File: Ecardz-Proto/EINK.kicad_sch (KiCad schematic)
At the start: 28 parts, among them J2 Conn_01x26, Q1 CSD16327Q3

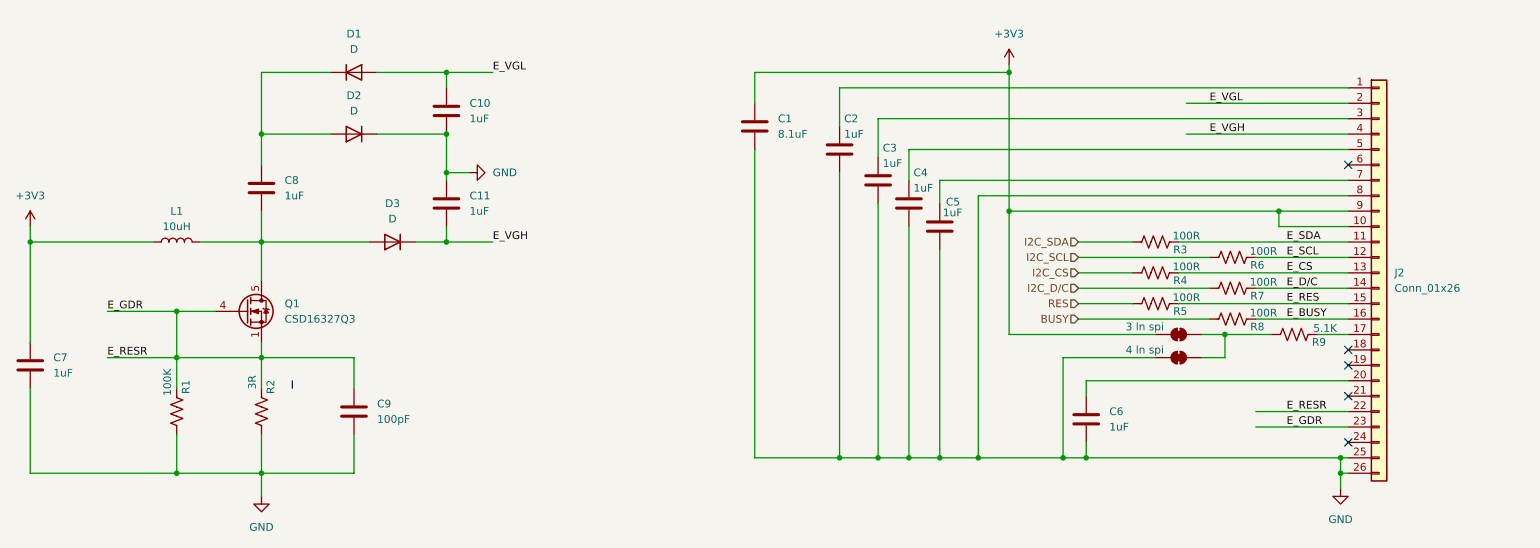
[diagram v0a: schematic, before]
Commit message: upated E-ink schematic
should be done - just missing inductor footprint
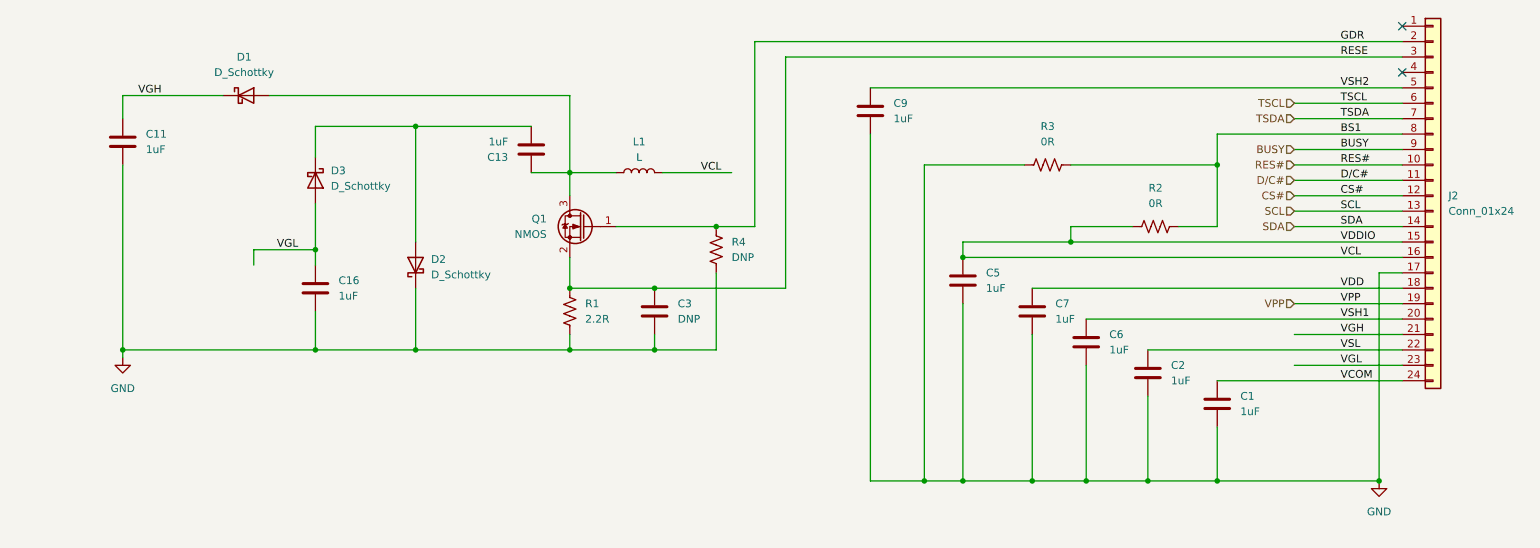
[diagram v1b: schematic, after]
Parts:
- removed C10, C4, C8: 1uF, symbol Device:C
- removed D1, D2, D3: D, symbol Device:D
- removed J2: Conn_01x26, symbol Connector_Generic:Conn_01x26
- removed JP1: 3 ln spi, symbol Jumper:SolderJumper_2_Bridged
- removed JP2: 4 ln spi, symbol Jumper:SolderJumper_2_Bridged
- removed Q1: CSD16327Q3, Package_SON:VSON-8_3.3x3.3mm_P0.65mm_NexFET, symbol Transistor_FET:CSD16327Q3
- removed R5, R6, R7, R8: 100R, symbol Device:R_US
- removed R9: 5.1K, symbol Device:R_US
- added C13, C16: 1uF, Capacitor_SMD:C_0603_1608Metric_Pad1.08x0.95mm_HandSolder, symbol Device:C
- added D1, D2, D3: D_Schottky, Diode_SMD:D_SOD-123, symbol Device:D_Schottky
- added J2: Conn_01x24, Connector_FFC-FPC:TE_2-1734839-4_1x24-1MP_P0.5mm_Horizontal, symbol Connector_Generic:Conn_01x24
- added Q1: NMOS, Package_TO_SOT_SMD:SOT-23, symbol Device:Q_NMOS_Depletion_GSD
- C1: value 8.1uF -> 1uF; footprint (none) -> Capacitor_SMD:C_0603_1608Metric_Pad1.08x0.95mm_HandSolder; MANUFACTURER PART NUMBER (none) -> CC0603KRX5R8BB105
- C11, C2, C5, C6, C7: footprint (none) -> Capacitor_SMD:C_0603_1608Metric_Pad1.08x0.95mm_HandSolder; MANUFACTURER PART NUMBER (none) -> CC0603KRX5R8BB105
- C3: value 1uF -> DNP; footprint (none) -> Capacitor_SMD:C_0603_1608Metric_Pad1.08x0.95mm_HandSolder; MANUFACTURER PART NUMBER (none) -> 100pF
- C9: value 100pF -> 1uF; footprint (none) -> Capacitor_SMD:C_0603_1608Metric_Pad1.08x0.95mm_HandSolder; MANUFACTURER PART NUMBER (none) -> CC0603KRX5R8BB105
- L1: value 10uH -> L; footprint (none) -> Inductor_SMD:L_Neosid_SM-PIC0602H; MANUFACTURER PART NUMBER (none) -> CDRH5D18NP-470NC
- R1: value 100K -> 2.2R; footprint (none) -> Resistor_SMD:R_0603_1608Metric_Pad0.98x0.95mm_HandSolder; MANUFACTURER PART NUMBER (none) -> RC0603FR-072R2L
- R2: value 3R -> 0R; footprint (none) -> Resistor_SMD:R_0603_1608Metric_Pad0.98x0.95mm_HandSolder; MANUFACTURER PART NUMBER (none) -> RC0603JR-070RL
- R3: value 100R -> 0R; footprint (none) -> Resistor_SMD:R_0603_1608Metric_Pad0.98x0.95mm_HandSolder; MANUFACTURER PART NUMBER (none) -> RC0603JR-070RL
- R4: value 100R -> DNP; footprint (none) -> Resistor_SMD:R_0603_1608Metric_Pad0.98x0.95mm_HandSolder; MANUFACTURER PART NUMBER (none) -> 100kR
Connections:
- net E_CS is gone; now on net GND: R4.2
- net E_VGH is gone; now on net GND: C11.2
- net I2C_SDA is gone; now on net GND: R3.1
- net BUSY: now also J2.9 (Pin_9)
- net GND: now also C1.2, R1.2, C16.2, D2.1 (K), J2.17 (Pin_17); no longer C1.1, C11.1, R1.1, R2.1
- net VCL: now reaches C5.1
- net VCL: now also L1.2, R2.1, J2.15 (Pin_15), J2.16 (Pin_16)
- net VSH1: now reaches C6.1
- net VSH1: now also J2.20 (Pin_20)
- net VSL: now reaches C2.1
- net VSL: now also J2.22 (Pin_22)
- net RESE: now reaches C3.1
- net RESE: now also R1.1, J2.3 (Pin_3), Q1.2 (S)
- removed net +3V3: C1.2, C7.1, L1.1
- removed net E_GDR: C9.1, R1.2, R2.2
- net E_SDA renamed BS1
- net BS1: now also R2.2, J2.8 (Pin_8)
- net I2C_CS renamed GDR
- net GDR: now also J2.2 (Pin_2), Q1.1 (G)
- new net: C13.1, D1.2 (A), L1.1, Q1.3 (D)
- new net: C13.2, D2.2 (A), D3.1 (K)
- new net CS#: J2.12 (Pin_12)
- new net D/C#: J2.11 (Pin_11)
- new net RES#: J2.10 (Pin_10)
- new net SCL: J2.13 (Pin_13)
- new net SDA: J2.14 (Pin_14)
- new net TSCL: J2.6 (Pin_6)
- new net TSDA: J2.7 (Pin_7)
- new net VCOM: C1.1, J2.24 (Pin_24)
- new net VDD: C7.1, J2.18 (Pin_18)
- new net VGH: C11.1, D1.1 (K), J2.21 (Pin_21)
- new net VGL: C16.1, D3.2 (A), J2.23 (Pin_23)
- new net VPP: J2.19 (Pin_19)
- new net VSH2: C9.1, J2.5 (Pin_5)
- no-connect marks 5 -> 2

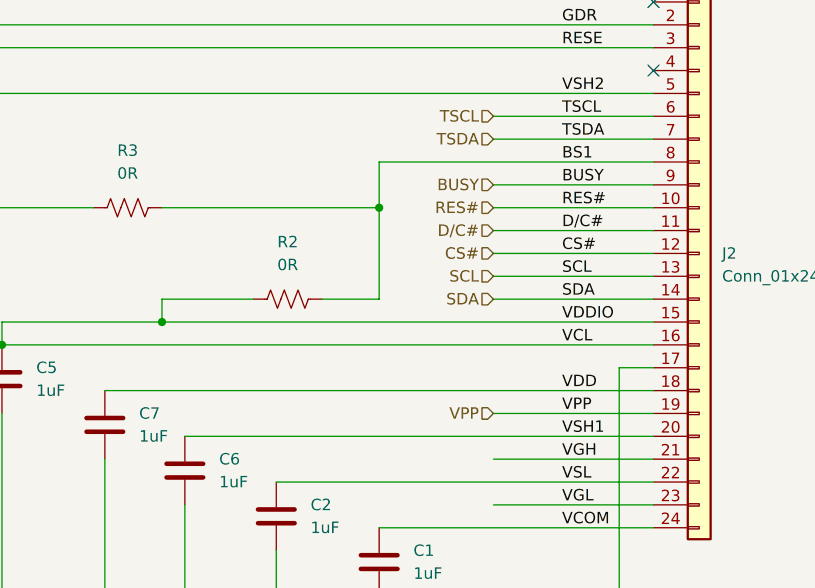
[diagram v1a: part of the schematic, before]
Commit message: added STM and rpi pin connections.
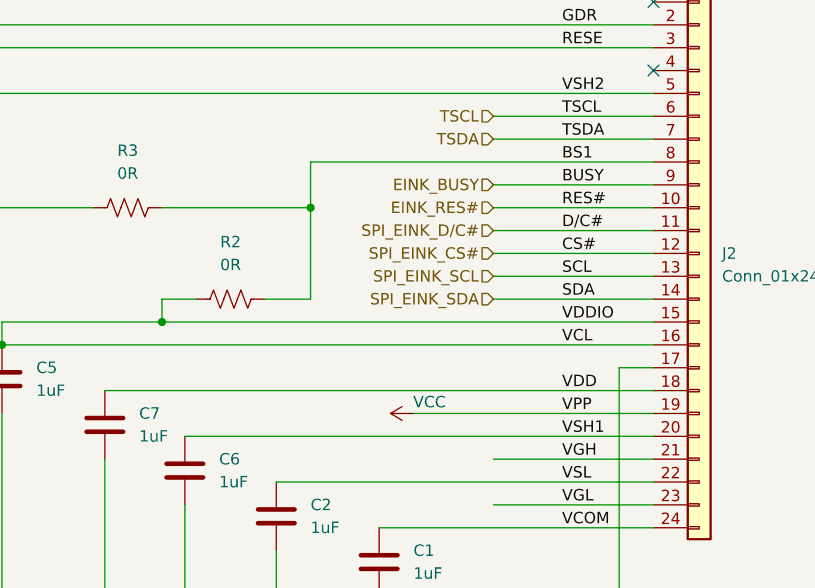
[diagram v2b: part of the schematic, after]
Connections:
- net BUSY renamed EINK_BUSY
- net CS# renamed SPI_EINK_CS#
- net D/C# renamed SPI_EINK_D/C#
- net RES# renamed EINK_RES#
- net SCL renamed SPI_EINK_SCL
- net SDA renamed SPI_EINK_SDA
- net VPP renamed VCC
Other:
- moved on the sheet: R2
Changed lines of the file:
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@@
 	)
 	(junction
+		(at 220.98 49.53)
+		(diameter 0)
+		(color 0 0 0 0)
+	)
+	(junction
 		(at 96.52 80.01)
 		(diameter 0)
@@
 	)
 	(junction
-		(at 228.6 49.53)
-		(diameter 0)
-		(color 0 0 0 0)
-	)
-	(junction
 		(at 255.27 101.6)
 		(diameter 0)
@@
 	(wire
 		(pts
-			(xy 214.63 59.69) (xy 204.47 59.69)
+			(xy 208.28 59.69) (xy 204.47 59.69)
 		)
 		(stroke
@@
 	(wire
 		(pts
-			(xy 204.47 49.53) (xy 228.6 49.53)
+			(xy 204.47 49.53) (xy 220.98 49.53)
 		)
 		(stroke
@@
 	(wire
 		(pts
-			(xy 241.3 72.39) (xy 259.08 72.39)
+			(xy 232.41 72.39) (xy 259.08 72.39)
 		)
 		(stroke
@@
 	(wire
 		(pts
-			(xy 228.6 44.45) (xy 259.08 44.45)
+			(xy 220.98 44.45) (xy 259.08 44.45)
 		)
 		(stroke
@@
 	(wire
 		(pts
-			(xy 222.25 59.69) (xy 228.6 59.69)
+			(xy 215.9 59.69) (xy 220.98 59.69)
 		)
 		(stroke
@@
 	(wire
 		(pts
-			(xy 228.6 44.45) (xy 228.6 49.53)
+			(xy 220.98 44.45) (xy 220.98 49.53)
 		)
 		(stroke
@@
 	(wire
 		(pts
-			(xy 228.6 59.69) (xy 228.6 49.53)
+			(xy 220.98 59.69) (xy 220.98 49.53)
 		)
 		(stroke
@@
 		)
 	)
-	(hierarchical_label "BUSY"
+	(hierarchical_label "EINK_BUSY"
 		(shape input)
 		(at 241.3 46.99 180)
@@
 		)
 	)
-	(hierarchical_label "SCL"
+	(hierarchical_label "SPI_EINK_SCL"
 		(shape input)
 		(at 241.3 57.15 180)
@@
 		)
 	)
-	(hierarchical_label "VPP"
-		(shape input)
-		(at 241.3 72.39 180)
-		(fields_autoplaced yes)
-		(effects
-			(font
-				(size 1.27 1.27)
-			)
-			(justify right)
-		)
-	)
 	(hierarchical_label "TSCL"
 		(shape input)
@@
 		)
 	)
-	(hierarchical_label "D{slash}C#"
+	(hierarchical_label "SPI_EINK_D{slash}C#"
 		(shape input)
 		(at 241.3 52.07 180)
@@
 		)
 	)
-	(hierarchical_label "CS#"
+	(hierarchical_label "SPI_EINK_CS#"
 		(shape input)
 		(at 241.3 54.61 180)
@@
 		)
 	)
-	(hierarchical_label "RES#"
+	(hierarchical_label "EINK_RES#"
 		(shape input)
 		(at 241.3 49.53 180)
@@
 		)
 	)
-	(hierarchical_label "SDA"
+	(hierarchical_label "SPI_EINK_SDA"
 		(shape input)
 		(at 241.3 59.69 180)
@@
 	(symbol
 		(lib_id "Device:R_US")
-		(at 218.44 59.69 90)
+		(at 212.09 59.69 90)
 		(unit 1)
 		(exclude_from_sim no)
@@
 		(fields_autoplaced yes)
 		(property "Reference" "R2"
-			(at 218.44 53.34 90)
+			(at 212.09 53.34 90)
 			(effects
 				(font
@@
 		)
 		(property "Value" "0R"
-			(at 218.44 55.88 90)
+			(at 212.09 55.88 90)
 			(effects
 				(font
@@
 		)
 		(property "Footprint" "Resistor_SMD:R_0603_1608Metric_Pad0.98x0.95mm_HandSolder"
-			(at 218.694 58.674 90)
+			(at 212.344 58.674 90)
 			(effects
 				(font
@@
 		)
 		(property "Datasheet" "https://www.yageo.com/upload/media/product/products/datasheet/rchip/PYu-RC_Group_51_RoHS_L_12.pdf"
-			(at 218.44 59.69 0)
+			(at 212.09 59.69 0)
 			(effects
 				(font
@@
 		)
 		(property "Description" "Resistor, US symbol"
-			(at 218.44 59.69 0)
+			(at 212.09 59.69 0)
 			(effects
 				(font
@@
 		)
 		(property "MANUFACTURER PART NUMBER" "RC0603JR-070RL"
-			(at 218.44 59.69 0)
+			(at 212.09 59.69 0)
 			(effects
 				(font
@@
 		)
 		(property "Sim.Device" ""
-			(at 218.44 59.69 0)
+			(at 212.09 59.69 0)
 			(effects
 				(font
@@
 		)
 		(property "Sim.Pins" ""
-			(at 218.44 59.69 0)
+			(at 212.09 59.69 0)
 			(effects
 				(font
@@
 		)
 		(property "Sim.Type" ""
-			(at 218.44 59.69 0)
+			(at 212.09 59.69 0)
 			(effects
 				(font
@@
 					(unit 1)
 				)
+			)
+		)
+	)
+	(symbol
+		(lib_id "power:VCC")
+		(at 232.41 72.39 90)
+		(unit 1)
+		(exclude_from_sim no)
+		(in_bom yes)
+		(on_board yes)
+		(dnp no)
+		(property "Reference" "#PWR012"
+			(at 236.22 72.39 0)
+			(effects
+				(font
+					(size 1.27 1.27)
+				)
+				(hide yes)
+			)
+		)
+		(property "Value" "VCC"
+			(at 234.188 71.12 90)
+			(effects
+				(font
+					(size 1.27 1.27)
+				)
+			)
+		)
+		(property "Footprint" ""
+			(at 232.41 72.39 0)
+			(effects
+				(font
+					(size 1.27 1.27)
+				)
+				(hide yes)
+			)
+		)
+		(property "Datasheet" ""
+			(at 232.41 72.39 0)
+			(effects
+				(font
+					(size 1.27 1.27)
+				)
+				(hide yes)
+			)
+		)
+		(property "Description" "Power symbol creates a global label with name \"VCC\""
+			(at 232.41 72.39 0)
+			(effects
+				(font
+					(size 1.27 1.27)
+				)
+				(hide yes)
+			)
+		)
+		(pin "1"
+		)
+		(instances
+			(project "Ecardz-Proto"
+				(path "/2adbba85-9270-4efb-857d-656bb51406ca/a8646e5d-e29c-4dc0-b052-9a424836bd67"
+					(reference "#PWR012")
+					(unit 1)
+				)

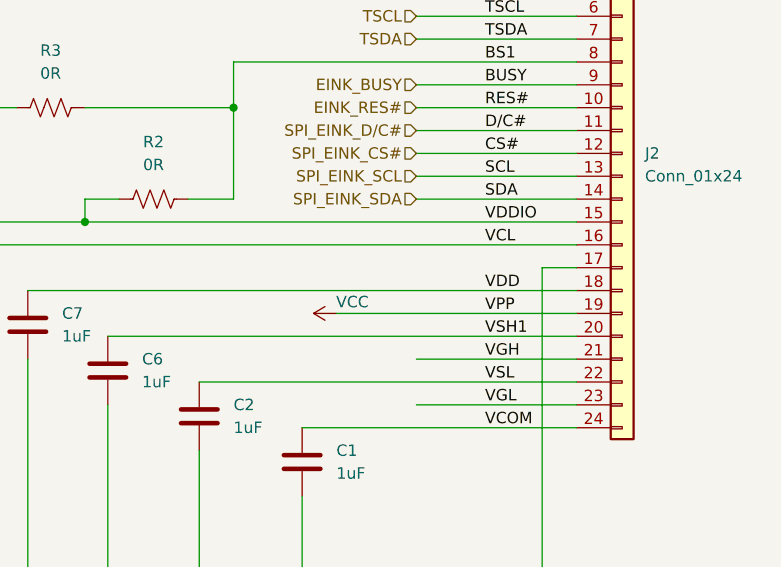
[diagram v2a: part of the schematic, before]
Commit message: made all supply voltages VDD rather than mix of VDD/VCC, added VDD measurement via STM32 internal ADC, put DNP jumper for VPP on E-ink connector, and made NFC VCC pin only connected to power if externally powered
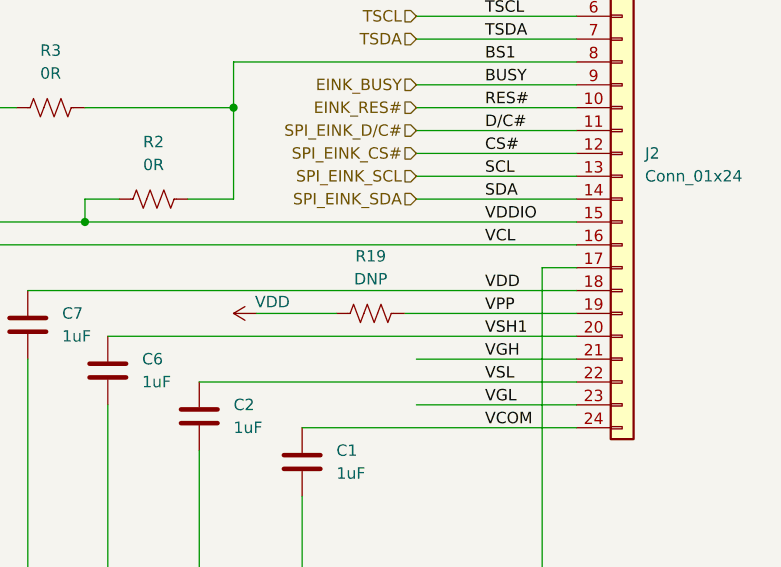
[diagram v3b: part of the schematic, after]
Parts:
- added R19: DNP, Resistor_SMD:R_0603_1608Metric_Pad0.98x0.95mm_HandSolder, symbol Device:R_US
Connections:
- net VDD: now also R19.1
- net VCC renamed VPP
- net VPP: now also R19.2
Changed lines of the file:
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@@
 	(wire
 		(pts
-			(xy 232.41 72.39) (xy 259.08 72.39)
-		)
-		(stroke
-			(width 0)
-			(type default)
-		)
-	)
-	(wire
-		(pts
 			(xy 96.52 43.18) (xy 96.52 62.23)
 		)
@@
 	(wire
 		(pts
+			(xy 240.03 72.39) (xy 259.08 72.39)
+		)
+		(stroke
+			(width 0)
+			(type default)
+		)
+	)
+	(wire
+		(pts
 			(xy 198.12 101.6) (xy 207.01 101.6)
 		)
@@
 	(wire
 		(pts
+			(xy 223.52 72.39) (xy 232.41 72.39)
+		)
+		(stroke
+			(width 0)
+			(type default)
+		)
+	)
+	(wire
+		(pts
 			(xy 135.89 77.47) (xy 135.89 80.01)
 		)
@@
 	)
 	(symbol
+		(lib_id "Device:R_US")
+		(at 236.22 72.39 90)
+		(unit 1)
+		(exclude_from_sim no)
+		(in_bom yes)
+		(on_board yes)
+		(dnp no)
+		(fields_autoplaced yes)
+		(property "Reference" "R19"
+			(at 236.22 66.04 90)
+			(effects
+				(font
+					(size 1.27 1.27)
+				)
+			)
+		)
+		(property "Value" "DNP"
+			(at 236.22 68.58 90)
+			(effects
+				(font
+					(size 1.27 1.27)
+				)
+			)
+		)
+		(property "Footprint" "Resistor_SMD:R_0603_1608Metric_Pad0.98x0.95mm_HandSolder"
+			(at 236.474 71.374 90)
+			(effects
+				(font
+					(size 1.27 1.27)
+				)
+				(hide yes)
+			)
+		)
+		(property "Datasheet" "https://www.yageo.com/upload/media/product/products/datasheet/rchip/PYu-RC_Group_51_RoHS_L_12.pdf"
+			(at 236.22 72.39 0)
+			(effects
+				(font
+					(size 1.27 1.27)
+				)
+				(hide yes)
+			)
+		)
+		(property "Description" "Resistor, US symbol"
+			(at 236.22 72.39 0)
+			(effects
+				(font
+					(size 1.27 1.27)
+				)
+				(hide yes)
+			)
+		)
+		(property "MANUFACTURER PART NUMBER" "RC0603JR-070RL"
+			(at 236.22 72.39 0)
+			(effects
+				(font
+					(size 1.27 1.27)
+				)
+				(hide yes)
+			)
+		)
+		(property "Sim.Device" ""
+			(at 236.22 72.39 0)
+			(effects
+				(font
+					(size 1.27 1.27)
+				)
+				(hide yes)
+			)
+		)
+		(property "Sim.Pins" ""
+			(at 236.22 72.39 0)
+			(effects
+				(font
+					(size 1.27 1.27)
+				)
+				(hide yes)
+			)
+		)
+		(property "Sim.Type" ""
+			(at 236.22 72.39 0)
+			(effects
+				(font
+					(size 1.27 1.27)
+				)
+				(hide yes)
+			)
+		)
+		(pin "1"
+		)
+		(pin "2"
+		)
+		(instances
+			(project "Ecardz-Proto"
+				(path "/2adbba85-9270-4efb-857d-656bb51406ca/a8646e5d-e29c-4dc0-b052-9a424836bd67"
+					(reference "R19")
+					(unit 1)
+				)
+			)
+		)
+	)
+	(symbol
 		(lib_id "Device:C")
 		(at 207.01 78.74 0)
@@
 	(symbol
 		(lib_id "power:VCC")
-		(at 232.41 72.39 90)
+		(at 223.52 72.39 90)
 		(unit 1)
 		(exclude_from_sim no)
@@
 		(dnp no)
 		(property "Reference" "#PWR012"
-			(at 236.22 72.39 0)
+			(at 227.33 72.39 0)
 			(effects
 				(font
@@
 			)
 		)
-		(property "Value" "VCC"
-			(at 234.188 71.12 90)
+		(property "Value" "VDD"
+			(at 225.298 71.12 90)
 			(effects
 				(font
@@
 		)
 		(property "Footprint" ""
-			(at 232.41 72.39 0)
+			(at 223.52 72.39 0)
 			(effects
 				(font
@@
 		)
 		(property "Datasheet" ""
-			(at 232.41 72.39 0)
+			(at 223.52 72.39 0)
 			(effects
 				(font
@@
 		)
 		(property "Description" "Power symbol creates a global label with name \"VCC\""
-			(at 232.41 72.39 0)
+			(at 223.52 72.39 0)
 			(effects
 				(font

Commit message: board outline
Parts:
- removed R19: DNP, Resistor_SMD:R_0603_1608Metric_Pad0.98x0.95mm_HandSolder, symbol Device:R_US
- added TP7: TestPoint, TestPoint:TestPoint_Pad_1.0x1.0mm, symbol Connector:TestPoint
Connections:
- net BS1: now also J2.17 (Pin_17); no longer J2.8 (Pin_8)
- net EINK_BUSY: now also J2.16 (Pin_16); no longer J2.9 (Pin_9)
- net EINK_RES#: now also J2.15 (Pin_15); no longer J2.10 (Pin_10)
- net GDR: now also J2.23 (Pin_23); no longer J2.2 (Pin_2)
- net GND: now also J2.8 (Pin_8); no longer J2.17 (Pin_17)
- net RESE: now also J2.22 (Pin_22); no longer J2.3 (Pin_3)
- net SPI_EINK_CS#: now also J2.13 (Pin_13); no longer J2.12 (Pin_12)
- net SPI_EINK_D/C#: now also J2.14 (Pin_14); no longer J2.11 (Pin_11)
- net SPI_EINK_SCL: now also J2.12 (Pin_12); no longer J2.13 (Pin_13)
- net SPI_EINK_SDA: now also J2.11 (Pin_11); no longer J2.14 (Pin_14)
- net TSCL: now also J2.19 (Pin_19); no longer J2.6 (Pin_6)
- net TSDA: now also J2.18 (Pin_18); no longer J2.7 (Pin_7)
- net VCOM: now also J2.1 (Pin_1); no longer J2.24 (Pin_24)
- net VDD: now also C5.1, J2.10 (Pin_10), J2.9 (Pin_9), L1.2, R2.1; no longer C7.1, J2.18 (Pin_18)
- net VGH: now also J2.4 (Pin_4); no longer J2.21 (Pin_21)
- net VGL: now also J2.2 (Pin_2); no longer J2.23 (Pin_23)
- net VPP: now also J2.6 (Pin_6), TP7.1; no longer J2.19 (Pin_19)
- net VSH1: now also J2.5 (Pin_5); no longer J2.20 (Pin_20)
- net VSH2: now also J2.20 (Pin_20); no longer J2.5 (Pin_5)
- net VSL: now also J2.3 (Pin_3); no longer J2.22 (Pin_22)
- removed net VCL: C5.1, J2.15 (Pin_15), J2.16 (Pin_16), L1.2, R2.1
- new net VDD_1.8V: C7.1, J2.7 (Pin_7)

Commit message: updated inductor
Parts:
- L1: footprint Inductor_SMD:L_Neosid_SM-PIC0602H -> parts-lib:CDRH5D18
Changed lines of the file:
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@@
 			)
 		)
-		(property "Footprint" "Inductor_SMD:L_Neosid_SM-PIC0602H"
+		(property "Footprint" "parts-lib:CDRH5D18"
 			(at 133.35 50.8 0)
 			(effects
